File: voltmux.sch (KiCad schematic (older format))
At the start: 0 parts

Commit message: Work on Voltage Sheet
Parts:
- added C?: 0.1uF, symbol Device:C_Small
- added J?: Conn_02x07_Counter_Clockwise, symbol Connector_Generic:Conn_02x07_Counter_Clockwise
- added R? (x2): 360k, symbol Device:R
- added R?: 200k, symbol Device:R
- added R? (x4): 100k, symbol Device:R
- added R?: 330k, symbol Device:R
- added R? (x3): 500k, symbol Device:R
- added R? (x3): 560k, symbol Device:R
- added R? (x2): 47k, symbol Device:R
- added R? (x2): 39.2k, symbol Device:R
- added R? (x2): 30k, symbol Device:R
- added R? (x4): R, symbol Device:R
- added R?: 25k, symbol Device:R
- added R? (x2): 33.2k, symbol Device:R
- added U?: CD74HC4067SM, Package_SO:SSOP-24_5.3x8.2mm_P0.65mm, symbol 74xx:CD74HC4067SM
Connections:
- new net +5V: C?.1, U?.24 (VCC)
- new net Cell10_P: J?.11 (Pin_11), R?.1
- new net Cell10_Sense: R?.1, R?.1, R?.2, U?.22 (I9)
- new net Cell11_P: J?.12 (Pin_12), R?.1
- new net Cell11_Sense: R?.1, R?.2, U?.21 (I10)
- new net Cell12_P: J?.13 (Pin_13), R?.1
- new net Cell12_Sense: R?.1, R?.2, U?.20 (I11)
- new net Cell1_P: J?.2 (Pin_2), U?.9 (I0)
- new net Cell2_P: J?.3 (Pin_3), R?.1
- new net Cell2_Sense: R?.1, R?.2, U?.8 (I1)
- new net Cell3_P: J?.4 (Pin_4), R?.1
- new net Cell3_Sense: R?.1, R?.2, U?.7 (I2)
- new net Cell4_P: J?.5 (Pin_5), R?.1
- new net Cell4_Sense: R?.1, R?.2, U?.6 (I3)
- new net Cell5_P: J?.6 (Pin_6), R?.1
- new net Cell5_Sense: R?.1, R?.1, R?.2, U?.5 (I4)
- new net Cell6_P: J?.7 (Pin_7), R?.1
- new net Cell6_Sense: R?.1, R?.2, U?.4 (I5)
- new net Cell7_P: J?.8 (Pin_8), R?.1
- new net Cell7_Sense: R?.1, R?.1, R?.2, U?.3 (I6)
- new net Cell8_P: J?.9 (Pin_9), R?.1
- new net Cell8_Sense: R?.1, R?.1, R?.2, U?.2 (I7)
- new net Cell9_P: J?.10 (Pin_10), R?.1
- new net Cell9_Sense: R?.1, R?.1, R?.2, U?.23 (I8)
- new net GND: C?.2, J?.1 (Pin_1), R?.2, R?.2, R?.2, R?.2, R?.2, R?.2, R?.2, R?.2, R?.2, R?.2, R?.2, R?.2, R?.2, R?.2, R?.2, R?.2, U?.12 (GND), U?.16 (I15), U?.17 (I14), U?.18 (I13), U?.19 (I12)
- no-connect marks 0 -> 1
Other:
- note added: "* Through resistance of Analogue Mux is around 60\n Ohms and connects to ADC\n which has input impedence of about 10M Ohm"

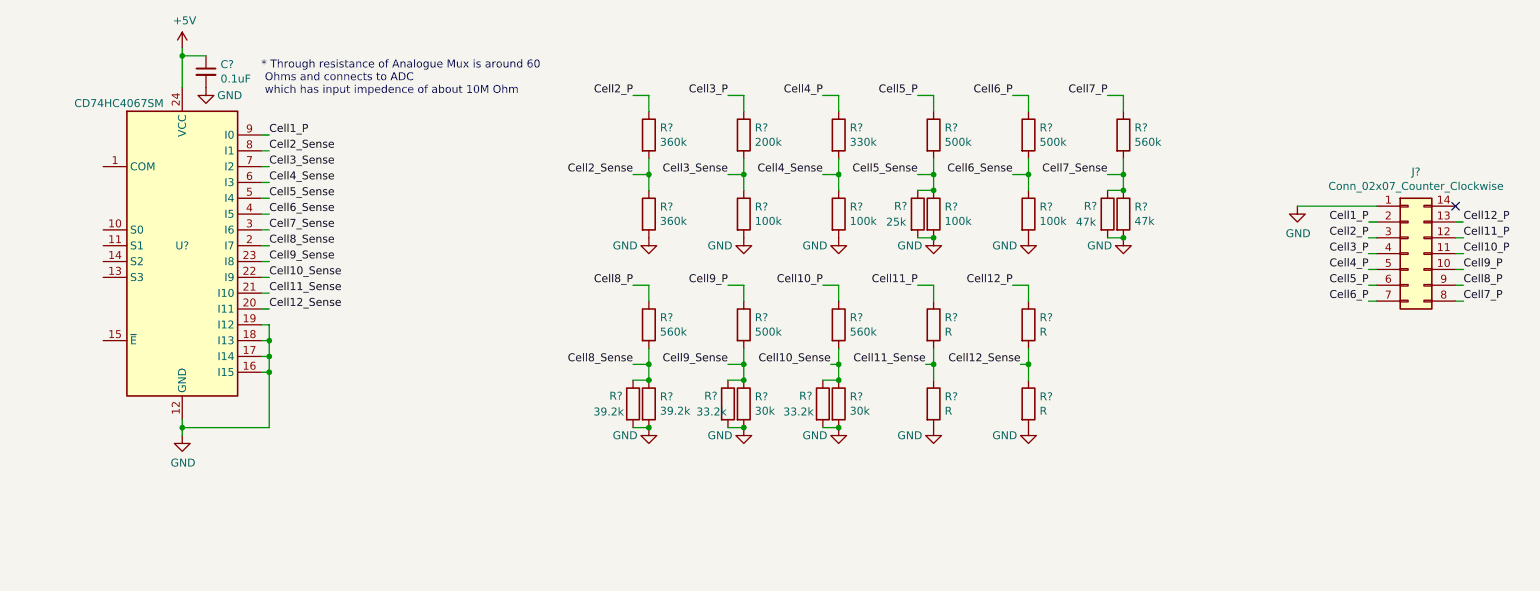
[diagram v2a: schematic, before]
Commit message: Finished Voltage divider network
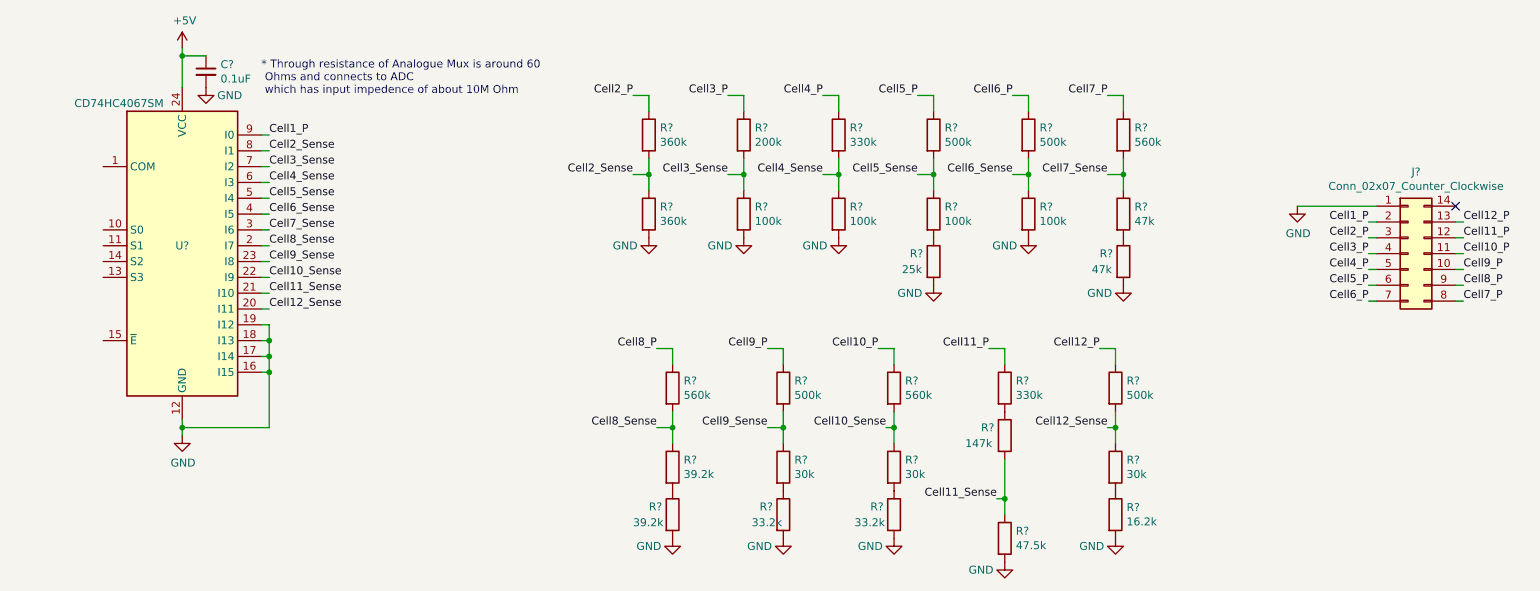
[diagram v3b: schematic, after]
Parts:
- added R?: 147k, symbol Device:R
- added R?: 16.2k, symbol Device:R
- R?: value R -> 330k
- R?: value R -> 47.5k
- R?: value R -> 500k
- R?: value R -> 30k
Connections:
- net Cell10_Sense: no longer R?.1
- net Cell11_Sense: now also R?.2; no longer R?.2
- net Cell5_Sense: no longer R?.1
- net Cell7_Sense: no longer R?.1
- net Cell8_Sense: no longer R?.1
- net Cell9_Sense: no longer R?.1
- net GND: now also R?.2; no longer R?.2, R?.2, R?.2, R?.2, R?.2, R?.2
- new net: R?.1, R?.2 (x7)
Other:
- moved on the sheet: R?

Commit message: Finished voltage sense sheet
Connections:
- net COM: now reaches U?.1 (COM)
- net S0: now reaches U?.10 (S0)
- net S1: now reaches U?.11 (S1)
- net S3: now reaches U?.13 (S3)
- net S2: now reaches U?.14 (S2)
- net ~Enable~: now reaches U?.15 (~E)
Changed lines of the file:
@@
 	1    0    0    -1
 $EndComp
+Text HLabel 1800 2250 0    50   Input ~ 0
+S0
+Text HLabel 1800 2350 0    50   Input ~ 0
+S1
+Text HLabel 1800 2450 0    50   Input ~ 0
+S2
+Text HLabel 1800 2550 0    50   Input ~ 0
+S3
+Wire Wire Line
+	1800 2550 1850 2550
+Wire Wire Line
+	1800 2450 1850 2450
+Wire Wire Line
+	1800 2350 1850 2350
+Wire Wire Line
+	1800 2250 1850 2250
+Text HLabel 1800 1850 0    50   BiDi ~ 0
+COM
+Wire Wire Line
+	1800 1850 1850 1850
+Text HLabel 1800 2950 0    50   Input ~ 0
+~Enable~
+Wire Wire Line
+	1800 2950 1850 2950
 $EndSCHEMATC

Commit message: Think I just added labels?
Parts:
- gave numbers to parts that had none: 32

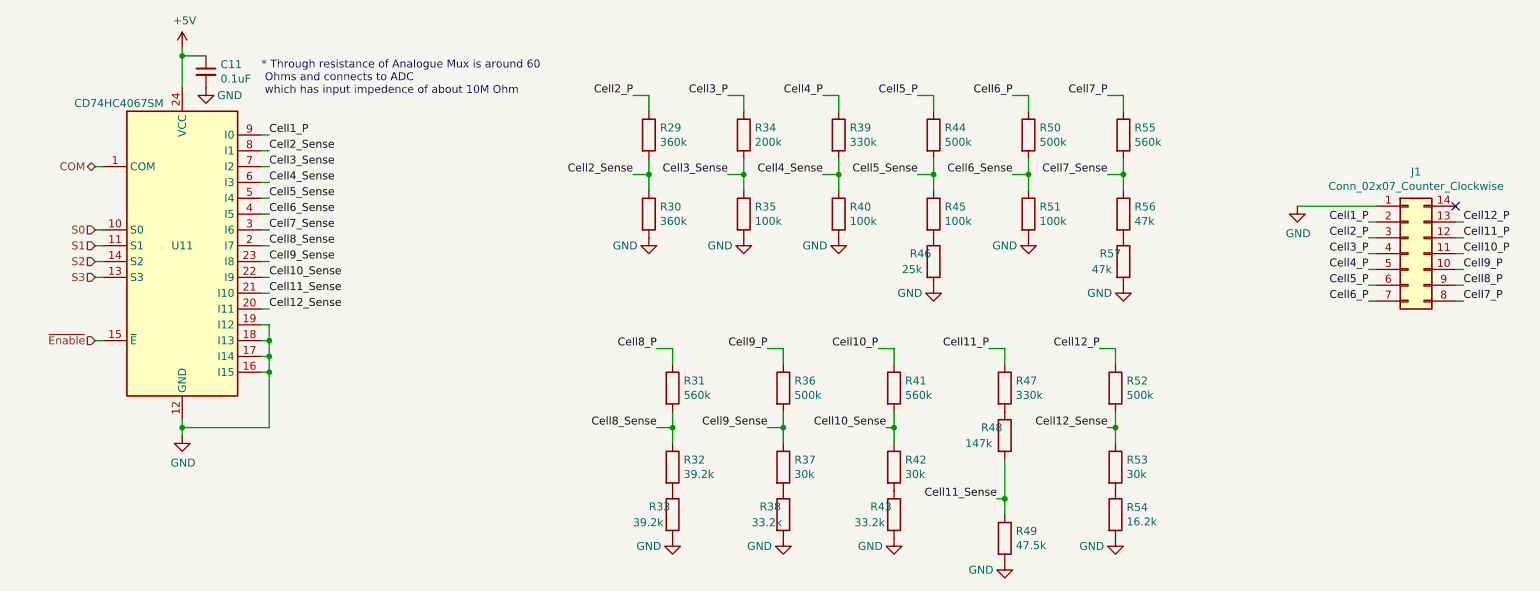
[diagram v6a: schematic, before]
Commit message: Added buttons + redid numbering
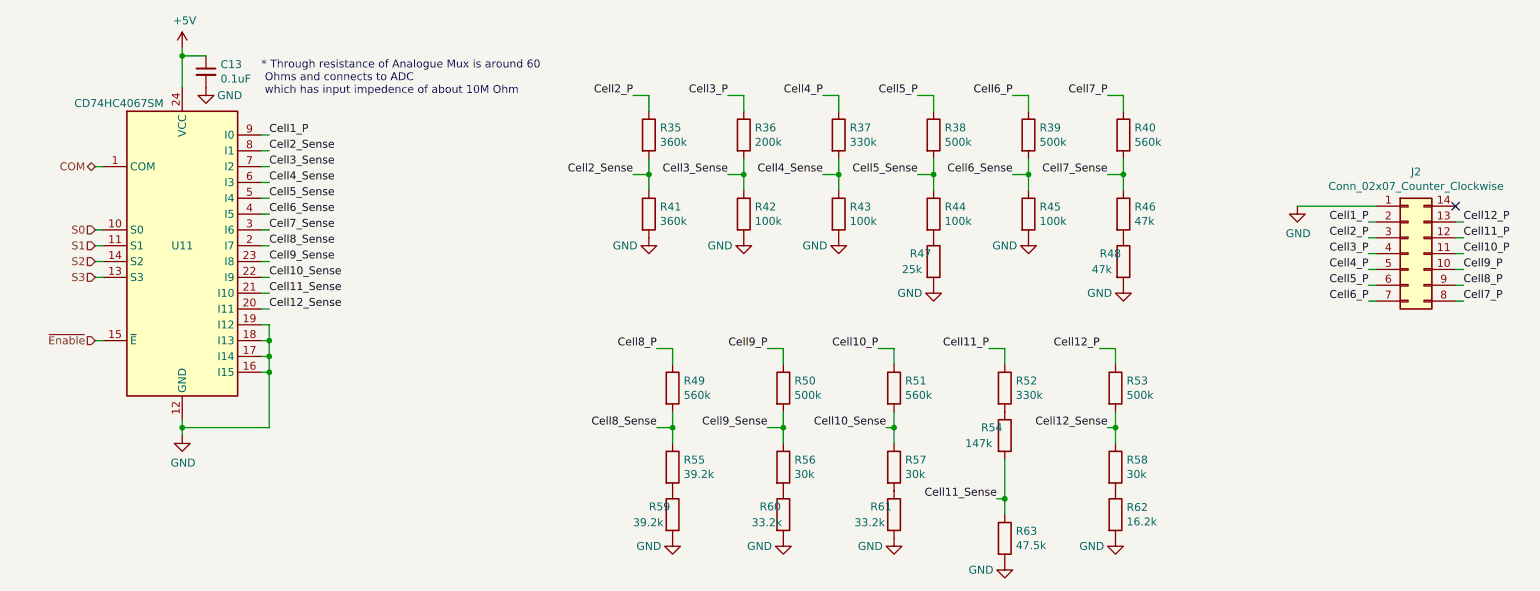
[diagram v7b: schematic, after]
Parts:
- renumbered C11 to C13, J1 to J2, R29 to R35, R34 to R36, R39 to R37, R44 to R38, R50 to R39, R55 to R40, R30 to R41, R35 to R42, R40 to R43, R45 to R44, R51 to R45, R56 to R46, R46 to R47, R57 to R48, R31 to R49, R36 to R50, R41 to R51, R47 to R52, R52 to R53, R48 to R54, R32 to R55, R37 to R56, R42 to R57, R53 to R58, R33 to R59, R38 to R60, R43 to R61, R54 to R62, R49 to R63

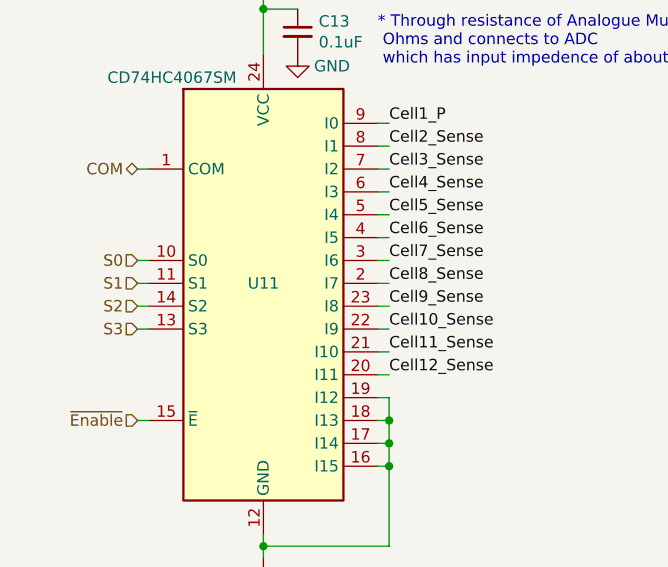
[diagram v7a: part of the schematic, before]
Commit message: Added most footprints
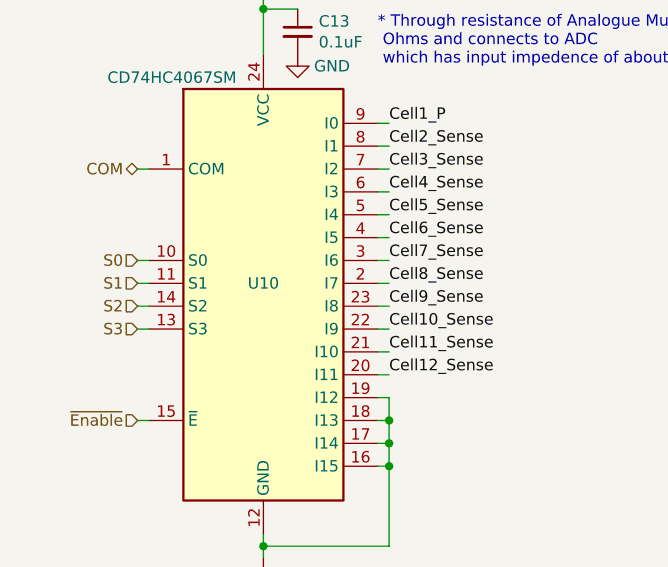
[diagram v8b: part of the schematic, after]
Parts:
- C13: footprint (none) -> Capacitor_SMD:C_1206_3216Metric
- J2: footprint (none) -> Connector_PinHeader_2.54mm:PinHeader_2x07_P2.54mm_Vertical
- R35, R36, R37, R38, R39, R40, R41, R42, R43, R44, R45, R46, R47, R48, R49, R50, R51, R52, R53, R54, R55, R56, R57, R58, R59, R60, R61, R62, R63: footprint (none) -> Resistor_SMD:R_0603_1608Metric_Pad1.05x0.95mm_HandSolder
- renumbered U11 to U10
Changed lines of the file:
@@
 $EndDescr
 $Comp
-L 74xx:CD74HC4067SM U11
+L 74xx:CD74HC4067SM U10
 U 1 1 5F5516A3
 P 2350 2350
-F 0 "U11" H 2350 2350 50  0000 C CNN
+F 0 "U10" H 2350 2350 50  0000 C CNN
 F 1 "CD74HC4067SM" H 1950 3250 50  0000 C CNN
 F 2 "Package_SO:SSOP-24_5.3x8.2mm_P0.65mm" H 3400 1350 50  0001 C CIN
@@
 F 0 "C13" H 2592 1296 50  0000 L CNN
 F 1 "0.1uF" H 2592 1205 50  0000 L CNN
-F 2 "" H 2500 1250 50  0001 C CNN
+F 2 "Capacitor_SMD:C_1206_3216Metric" H 2500 1250 50  0001 C CNN
 F 3 "~" H 2500 1250 50  0001 C CNN
 	1    2500 1250
@@
 F 0 "J2" H 10150 2917 50  0000 C CNN
 F 1 "Conn_02x07_Counter_Clockwise" H 10150 2826 50  0000 C CNN
-F 2 "" H 10100 2400 50  0001 C CNN
+F 2 "Connector_PinHeader_2.54mm:PinHeader_2x07_P2.54mm_Vertical" H 10100 2400 50  0001 C CNN
 F 3 "~" H 10100 2400 50  0001 C CNN
 	1    10100 2400
@@
 F 0 "R35" H 5370 1696 50  0000 L CNN
 F 1 "360k" H 5370 1605 50  0000 L CNN
-F 2 "" V 5230 1650 50  0001 C CNN
+F 2 "Resistor_SMD:R_0603_1608Metric_Pad1.05x0.95mm_HandSolder" V 5230 1650 50  0001 C CNN
 F 3 "~" H 5300 1650 50  0001 C CNN
 	1    5300 1650
@@
 F 0 "R41" H 5370 2196 50  0000 L CNN
 F 1 "360k" H 5370 2105 50  0000 L CNN
-F 2 "" V 5230 2150 50  0001 C CNN
+F 2 "Resistor_SMD:R_0603_1608Metric_Pad1.05x0.95mm_HandSolder" V 5230 2150 50  0001 C CNN
 F 3 "~" H 5300 2150 50  0001 C CNN
 	1    5300 2150
@@
 F 0 "R36" H 5970 1696 50  0000 L CNN
 F 1 "200k" H 5970 1605 50  0000 L CNN
-F 2 "" V 5830 1650 50  0001 C CNN
+F 2 "Resistor_SMD:R_0603_1608Metric_Pad1.05x0.95mm_HandSolder" V 5830 1650 50  0001 C CNN
 F 3 "~" H 5900 1650 50  0001 C CNN
 	1    5900 1650
@@
 F 0 "R42" H 5970 2196 50  0000 L CNN
 F 1 "100k" H 5970 2105 50  0000 L CNN
-F 2 "" V 5830 2150 50  0001 C CNN
+F 2 "Resistor_SMD:R_0603_1608Metric_Pad1.05x0.95mm_HandSolder" V 5830 2150 50  0001 C CNN
 F 3 "~" H 5900 2150 50  0001 C CNN
 	1    5900 2150
@@
 F 0 "R37" H 6570 1696 50  0000 L CNN
 F 1 "330k" H 6570 1605 50  0000 L CNN
-F 2 "" V 6430 1650 50  0001 C CNN
+F 2 "Resistor_SMD:R_0603_1608Metric_Pad1.05x0.95mm_HandSolder" V 6430 1650 50  0001 C CNN
 F 3 "~" H 6500 1650 50  0001 C CNN
 	1    6500 1650
@@
 F 0 "R43" H 6570 2196 50  0000 L CNN
 F 1 "100k" H 6570 2105 50  0000 L CNN
-F 2 "" V 6430 2150 50  0001 C CNN
+F 2 "Resistor_SMD:R_0603_1608Metric_Pad1.05x0.95mm_HandSolder" V 6430 2150 50  0001 C CNN
 F 3 "~" H 6500 2150 50  0001 C CNN
 	1    6500 2150
@@
 F 0 "R38" H 7170 1696 50  0000 L CNN
 F 1 "500k" H 7170 1605 50  0000 L CNN
-F 2 "" V 7030 1650 50  0001 C CNN
+F 2 "Resistor_SMD:R_0603_1608Metric_Pad1.05x0.95mm_HandSolder" V 7030 1650 50  0001 C CNN
 F 3 "~" H 7100 1650 50  0001 C CNN
 	1    7100 1650
@@
 F 0 "R44" H 7170 2196 50  0000 L CNN
 F 1 "100k" H 7170 2105 50  0000 L CNN
-F 2 "" V 7030 2150 50  0001 C CNN
+F 2 "Resistor_SMD:R_0603_1608Metric_Pad1.05x0.95mm_HandSolder" V 7030 2150 50  0001 C CNN
 F 3 "~" H 7100 2150 50  0001 C CNN
 	1    7100 2150
@@
 F 0 "R39" H 7770 1696 50  0000 L CNN
 F 1 "500k" H 7770 1605 50  0000 L CNN
-F 2 "" V 7630 1650 50  0001 C CNN
+F 2 "Resistor_SMD:R_0603_1608Metric_Pad1.05x0.95mm_HandSolder" V 7630 1650 50  0001 C CNN
 F 3 "~" H 7700 1650 50  0001 C CNN
 	1    7700 1650
@@
 F 0 "R45" H 7770 2196 50  0000 L CNN
 F 1 "100k" H 7770 2105 50  0000 L CNN
-F 2 "" V 7630 2150 50  0001 C CNN
+F 2 "Resistor_SMD:R_0603_1608Metric_Pad1.05x0.95mm_HandSolder" V 7630 2150 50  0001 C CNN
 F 3 "~" H 7700 2150 50  0001 C CNN
 	1    7700 2150
@@
 F 0 "R40" H 8370 1696 50  0000 L CNN
 F 1 "560k" H 8370 1605 50  0000 L CNN
-F 2 "" V 8230 1650 50  0001 C CNN
+F 2 "Resistor_SMD:R_0603_1608Metric_Pad1.05x0.95mm_HandSolder" V 8230 1650 50  0001 C CNN
 F 3 "~" H 8300 1650 50  0001 C CNN
 	1    8300 1650
@@
 F 0 "R46" H 8370 2196 50  0000 L CNN
 F 1 "47k" H 8370 2105 50  0000 L CNN
-F 2 "" V 8230 2150 50  0001 C CNN
+F 2 "Resistor_SMD:R_0603_1608Metric_Pad1.05x0.95mm_HandSolder" V 8230 2150 50  0001 C CNN
 F 3 "~" H 8300 2150 50  0001 C CNN
 	1    8300 2150
@@
 F 0 "R49" H 5520 3296 50  0000 L CNN
 F 1 "560k" H 5520 3205 50  0000 L CNN
-F 2 "" V 5380 3250 50  0001 C CNN
+F 2 "Resistor_SMD:R_0603_1608Metric_Pad1.05x0.95mm_HandSolder" V 5380 3250 50  0001 C CNN
 F 3 "~" H 5450 3250 50  0001 C CNN
 	1    5450 3250
@@
 F 0 "R55" H 5520 3796 50  0000 L CNN
 F 1 "39.2k" H 5520 3705 50  0000 L CNN
-F 2 "" V 5380 3750 50  0001 C CNN
+F 2 "Resistor_SMD:R_0603_1608Metric_Pad1.05x0.95mm_HandSolder" V 5380 3750 50  0001 C CNN
 F 3 "~" H 5450 3750 50  0001 C CNN
 	1    5450 3750
@@
 F 0 "R50" H 6220 3296 50  0000 L CNN
 F 1 "500k" H 6220 3205 50  0000 L CNN
-F 2 "" V 6080 3250 50  0001 C CNN
+F 2 "Resistor_SMD:R_0603_1608Metric_Pad1.05x0.95mm_HandSolder" V 6080 3250 50  0001 C CNN
 F 3 "~" H 6150 3250 50  0001 C CNN
 	1    6150 3250
@@
 F 0 "R56" H 6220 3796 50  0000 L CNN
 F 1 "30k" H 6220 3705 50  0000 L CNN
-F 2 "" V 6080 3750 50  0001 C CNN
+F 2 "Resistor_SMD:R_0603_1608Metric_Pad1.05x0.95mm_HandSolder" V 6080 3750 50  0001 C CNN
 F 3 "~" H 6150 3750 50  0001 C CNN
 	1    6150 3750
@@
 F 0 "R51" H 6920 3296 50  0000 L CNN
 F 1 "560k" H 6920 3205 50  0000 L CNN
-F 2 "" V 6780 3250 50  0001 C CNN
+F 2 "Resistor_SMD:R_0603_1608Metric_Pad1.05x0.95mm_HandSolder" V 6780 3250 50  0001 C CNN
 F 3 "~" H 6850 3250 50  0001 C CNN
 	1    6850 3250
@@
 F 0 "R57" H 6920 3796 50  0000 L CNN
 F 1 "30k" H 6920 3705 50  0000 L CNN
-F 2 "" V 6780 3750 50  0001 C CNN
+F 2 "Resistor_SMD:R_0603_1608Metric_Pad1.05x0.95mm_HandSolder" V 6780 3750 50  0001 C CNN
 F 3 "~" H 6850 3750 50  0001 C CNN
 	1    6850 3750
@@
 F 0 "R52" H 7620 3296 50  0000 L CNN
 F 1 "330k" H 7620 3205 50  0000 L CNN
-F 2 "" V 7480 3250 50  0001 C CNN
+F 2 "Resistor_SMD:R_0603_1608Metric_Pad1.05x0.95mm_HandSolder" V 7480 3250 50  0001 C CNN
 F 3 "~" H 7550 3250 50  0001 C CNN
 	1    7550 3250
@@
 F 0 "R63" H 7620 4246 50  0000 L CNN
 F 1 "47.5k" H 7620 4155 50  0000 L CNN
-F 2 "" V 7480 4200 50  0001 C CNN
+F 2 "Resistor_SMD:R_0603_1608Metric_Pad1.05x0.95mm_HandSolder" V 7480 4200 50  0001 C CNN
 F 3 "~" H 7550 4200 50  0001 C CNN
 	1    7550 4200
@@
 F 0 "R53" H 8320 3296 50  0000 L CNN
 F 1 "500k" H 8320 3205 50  0000 L CNN
-F 2 "" V 8180 3250 50  0001 C CNN
+F 2 "Resistor_SMD:R_0603_1608Metric_Pad1.05x0.95mm_HandSolder" V 8180 3250 50  0001 C CNN
 F 3 "~" H 8250 3250 50  0001 C CNN
 	1    8250 3250
@@
 F 0 "R58" H 8320 3796 50  0000 L CNN
 F 1 "30k" H 8320 3705 50  0000 L CNN
-F 2 "" V 8180 3750 50  0001 C CNN
+F 2 "Resistor_SMD:R_0603_1608Metric_Pad1.05x0.95mm_HandSolder" V 8180 3750 50  0001 C CNN
 F 3 "~" H 8250 3750 50  0001 C CNN
 	1    8250 3750
@@
 F 0 "R47" H 6950 2500 50  0000 L CNN
 F 1 "25k" H 6900 2400 50  0000 L CNN
-F 2 "" V 7030 2450 50  0001 C CNN
+F 2 "Resistor_SMD:R_0603_1608Metric_Pad1.05x0.95mm_HandSolder" V 7030 2450 50  0001 C CNN
 F 3 "~" H 7100 2450 50  0001 C CNN
 	1    7100 2450
@@
 F 0 "R48" H 8150 2500 50  0000 L CNN
 F 1 "47k" H 8100 2400 50  0000 L CNN
-F 2 "" V 8230 2450 50  0001 C CNN
+F 2 "Resistor_SMD:R_0603_1608Metric_Pad1.05x0.95mm_HandSolder" V 8230 2450 50  0001 C CNN
 F 3 "~" H 8300 2450 50  0001 C CNN
 	1    8300 2450
@@
 F 0 "R59" H 5300 4100 50  0000 L CNN
 F 1 "39.2k" H 5200 4000 50  0000 L CNN
-F 2 "" V 5380 4050 50  0001 C CNN
+F 2 "Resistor_SMD:R_0603_1608Metric_Pad1.05x0.95mm_HandSolder" V 5380 4050 50  0001 C CNN
 F 3 "~" H 5450 4050 50  0001 C CNN
 	1    5450 4050
@@
 F 0 "R60" H 6000 4100 50  0000 L CNN
 F 1 "33.2k" H 5950 4000 50  0000 L CNN
-F 2 "" V 6080 4050 50  0001 C CNN
+F 2 "Resistor_SMD:R_0603_1608Metric_Pad1.05x0.95mm_HandSolder" V 6080 4050 50  0001 C CNN
 F 3 "~" H 6150 4050 50  0001 C CNN
 	1    6150 4050
@@
 F 0 "R61" H 6700 4100 50  0000 L CNN
 F 1 "33.2k" H 6600 4000 50  0000 L CNN
-F 2 "" V 6780 4050 50  0001 C CNN
+F 2 "Resistor_SMD:R_0603_1608Metric_Pad1.05x0.95mm_HandSolder" V 6780 4050 50  0001 C CNN
 F 3 "~" H 6850 4050 50  0001 C CNN
 	1    6850 4050
@@
 F 0 "R54" H 7400 3600 50  0000 L CNN
 F 1 "147k" H 7300 3500 50  0000 L CNN
-F 2 "" V 7480 3550 50  0001 C CNN
+F 2 "Resistor_SMD:R_0603_1608Metric_Pad1.05x0.95mm_HandSolder" V 7480 3550 50  0001 C CNN
 F 3 "~" H 7550 3550 50  0001 C CNN
 	1    7550 3550
@@
 F 0 "R62" H 8320 4096 50  0000 L CNN
 F 1 "16.2k" H 8320 4005 50  0000 L CNN
-F 2 "" V 8180 4050 50  0001 C CNN
+F 2 "Resistor_SMD:R_0603_1608Metric_Pad1.05x0.95mm_HandSolder" V 8180 4050 50  0001 C CNN
 F 3 "~" H 8250 4050 50  0001 C CNN
 	1    8250 4050
